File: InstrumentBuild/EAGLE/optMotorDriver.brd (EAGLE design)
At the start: 71.1 x 54.6 mm, 24 parts, among them U1 ARDUINOR3-DIMENSION

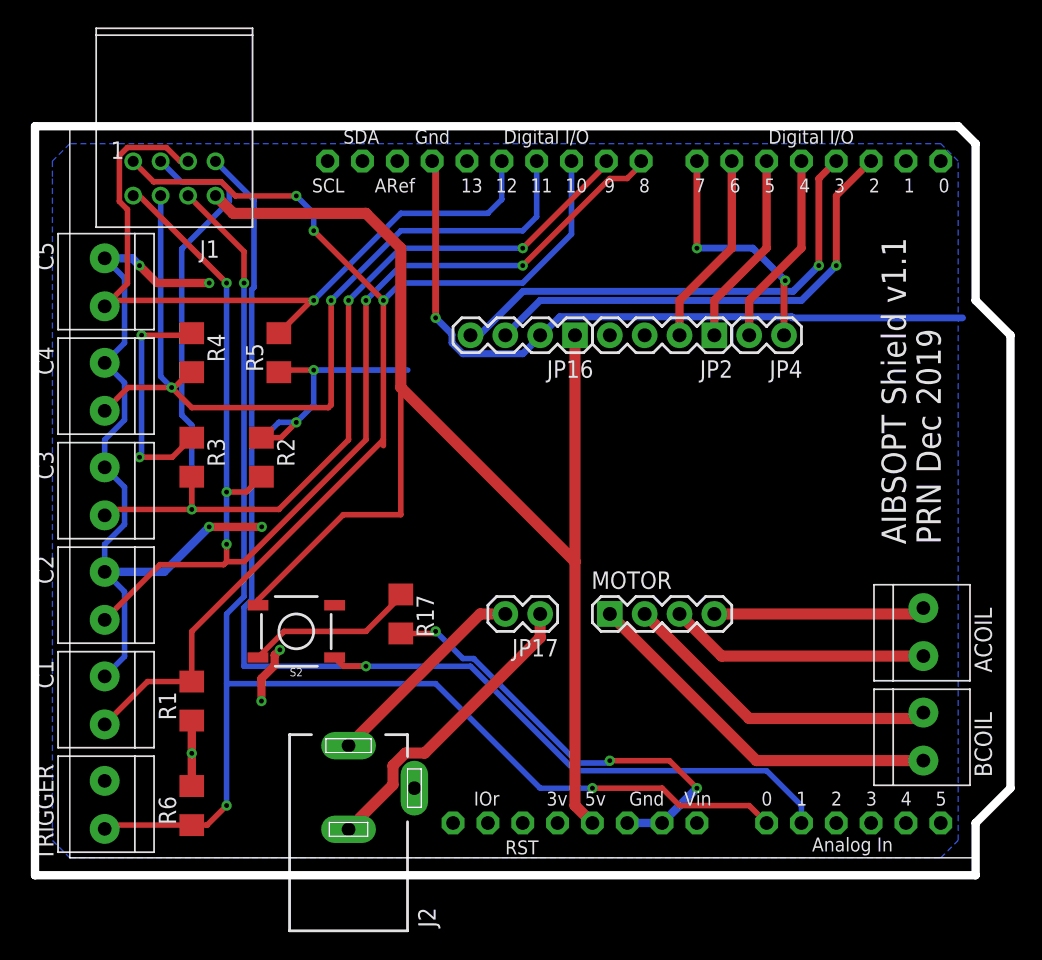
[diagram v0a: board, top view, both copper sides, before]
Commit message: Updated top silk, removed some layout corners and increased version to 1.2.
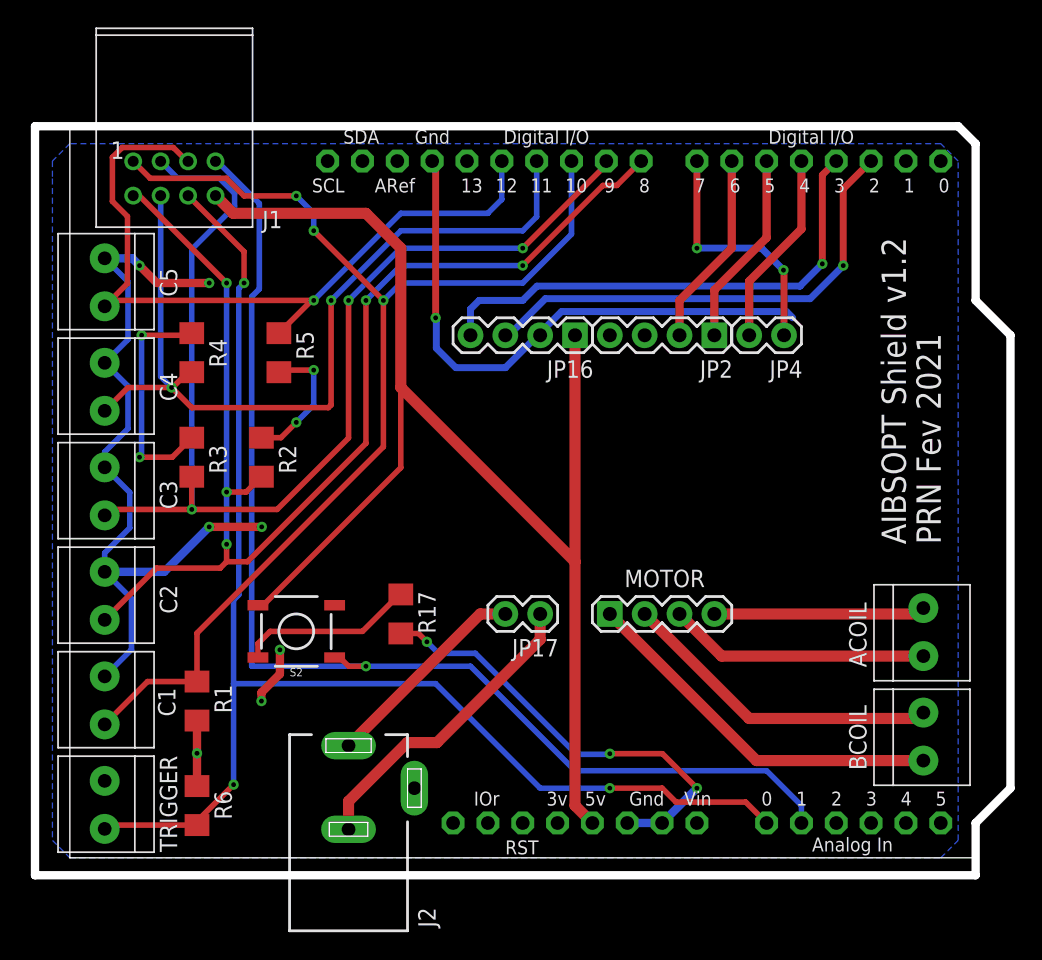
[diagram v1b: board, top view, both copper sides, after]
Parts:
- moved R1 0.38 mm to (42.3, 29.2)
- moved R6 0.38 mm to (42.3, 21.6)
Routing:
- net GND: track 188.5 -> 168.4 mm
- net VCC: track 101.9 -> 99.7 mm
- net DIR_IN: track 35.7 -> 36.8 mm
- net N$13: track 99.9 -> 98.9 mm
- net N$7: track 56.1 -> 56.7 mm
- net N$16: track 12.4 -> 12.9 mm
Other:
- board text added: "AIBSOPT Shield v1.2"
- board text added: "PRN Fev 2021"
- board text removed: "AIBSOPT Shield v1.1"
- board text removed: "PRN Dec 2019"
